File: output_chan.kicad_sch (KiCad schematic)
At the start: 12 parts, among them U4 MAX14917AFM+

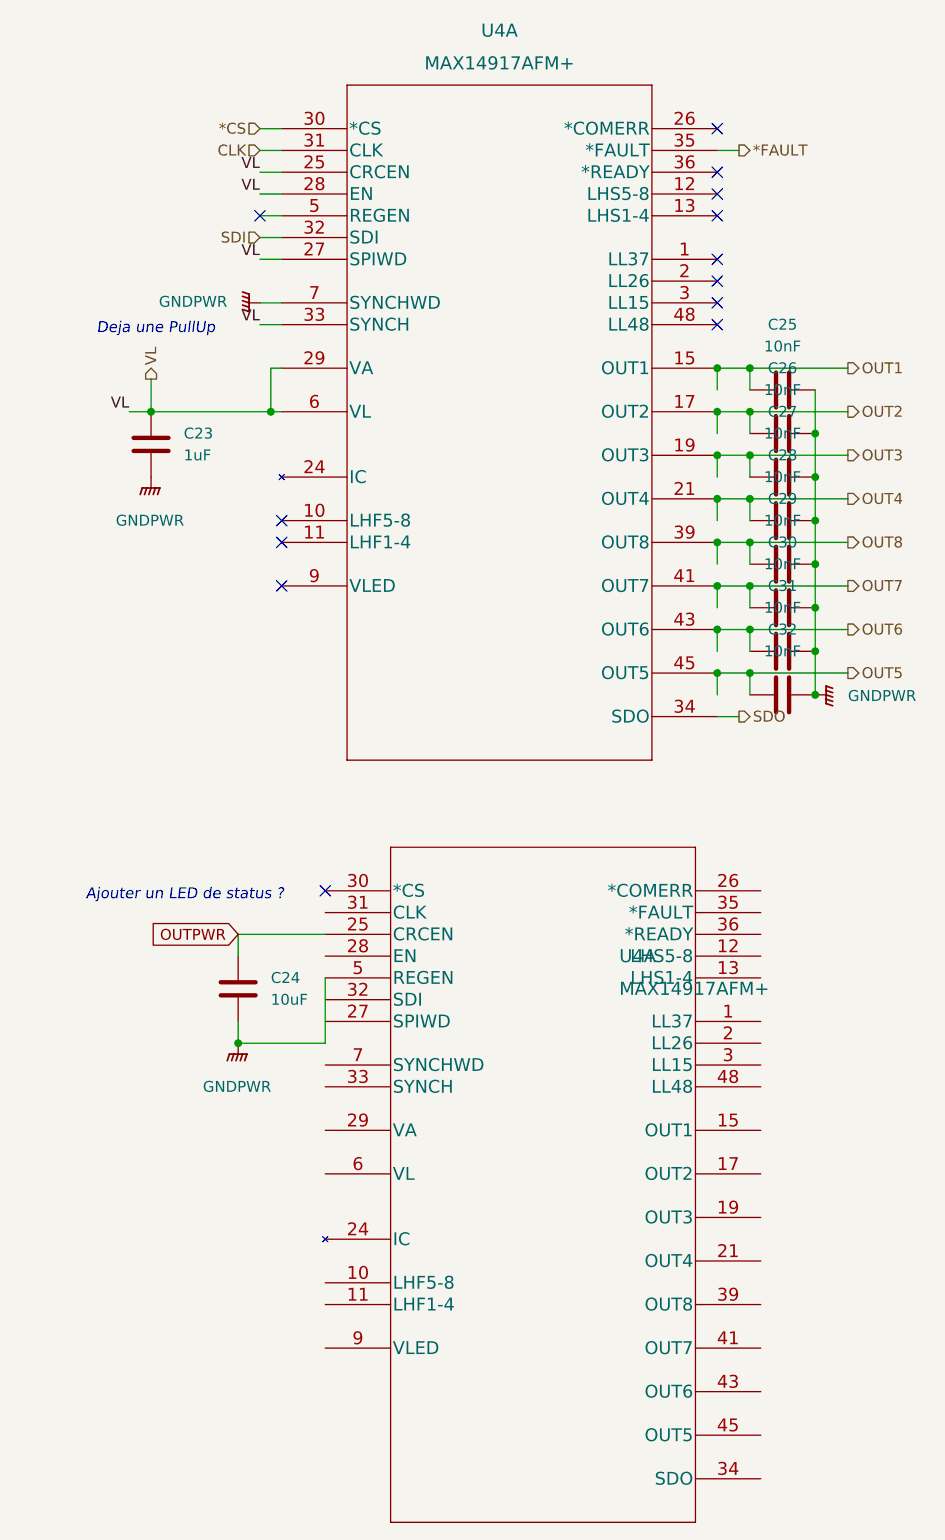
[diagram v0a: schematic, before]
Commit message: add MPGA and MPGB on a DB25 (isolated)
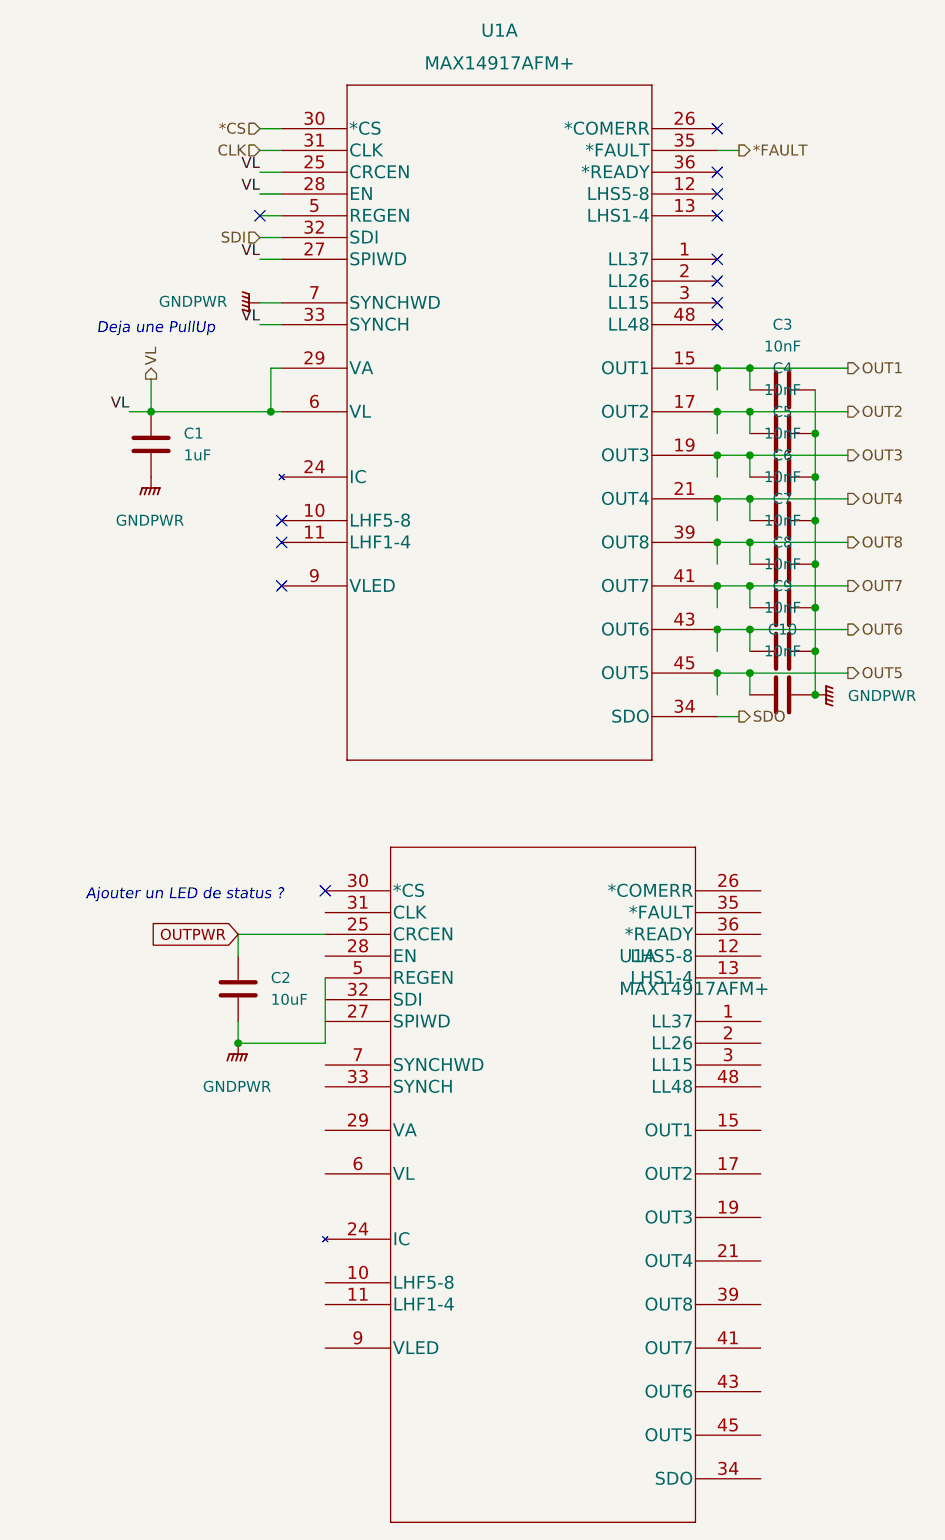
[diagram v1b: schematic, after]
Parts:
- renumbered C23 to C1, C32 to C10, C24 to C2, C25 to C3, C26 to C4, C27 to C5, C28 to C6, C29 to C7, C30 to C8, C31 to C9, U4 to U1
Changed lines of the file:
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@@
   (symbol (lib_id "power:GNDPWR") (at 189.23 109.22 90)
     (in_bom yes) (on_board yes) (fields_autoplaced)
-    (property "Reference" "#PWR023" (id 0) (at 194.31 109.22 0)
+    (property "Reference" "#PWR04" (id 0) (at 194.31 109.22 0)
       (effects (font (size 1.27 1.27)) hide)
     )
@@
   (symbol (lib_id "Device:C") (at 111.76 80.01 0)
     (in_bom yes) (on_board yes) (fields_autoplaced)
-    (property "Reference" "C23" (id 0) (at 115.57 78.7399 0)
+    (property "Reference" "C1" (id 0) (at 115.57 78.7399 0)
       (effects (font (size 1.27 1.27)) (justify left))
     )
@@
   (symbol (lib_id "power:GNDPWR") (at 111.76 83.82 0)
     (in_bom yes) (on_board yes) (fields_autoplaced)
-    (property "Reference" "#PWR020" (id 0) (at 111.76 88.9 0)
+    (property "Reference" "#PWR01" (id 0) (at 111.76 88.9 0)
       (effects (font (size 1.27 1.27)) hide)
     )
@@
   (symbol (lib_id "Maxim industrial IO:MAX14917AFM+") (at 127 43.18 0)
     (in_bom yes) (on_board yes) (fields_autoplaced)
-    (property "Reference" "U4" (id 0) (at 152.4 31.75 0)
+    (property "Reference" "U1" (id 0) (at 152.4 31.75 0)
       (effects (font (size 1.524 1.524)))
     )
@@
   (symbol (lib_id "Device:C") (at 185.42 83.82 90)
     (in_bom yes) (on_board yes) (fields_autoplaced)
-    (property "Reference" "C27" (id 0) (at 185.42 76.2 90))
+    (property "Reference" "C5" (id 0) (at 185.42 76.2 90))
     (property "Value" "10nF" (id 1) (at 185.42 78.74 90))
     (property "Footprint" "Capacitor_SMD:C_0603_1608Metric" (id 2) (at 189.23 82.8548 0)
@@
   (symbol (lib_id "Device:C") (at 185.42 88.9 90)
     (in_bom yes) (on_board yes) (fields_autoplaced)
-    (property "Reference" "C28" (id 0) (at 185.42 81.28 90))
+    (property "Reference" "C6" (id 0) (at 185.42 81.28 90))
     (property "Value" "10nF" (id 1) (at 185.42 83.82 90))
     (property "Footprint" "Capacitor_SMD:C_0603_1608Metric" (id 2) (at 189.23 87.9348 0)
@@
   (symbol (lib_id "Device:C") (at 185.42 78.74 90)
     (in_bom yes) (on_board yes) (fields_autoplaced)
-    (property "Reference" "C26" (id 0) (at 185.42 71.12 90))
+    (property "Reference" "C4" (id 0) (at 185.42 71.12 90))
     (property "Value" "10nF" (id 1) (at 185.42 73.66 90))
     (property "Footprint" "Capacitor_SMD:C_0603_1608Metric" (id 2) (at 189.23 77.7748 0)
@@
   (symbol (lib_id "Device:C") (at 185.42 104.14 90)
     (in_bom yes) (on_board yes) (fields_autoplaced)
-    (property "Reference" "C31" (id 0) (at 185.42 96.52 90))
+    (property "Reference" "C9" (id 0) (at 185.42 96.52 90))
     (property "Value" "10nF" (id 1) (at 185.42 99.06 90))
     (property "Footprint" "Capacitor_SMD:C_0603_1608Metric" (id 2) (at 189.23 103.1748 0)
@@
   (symbol (lib_id "power:GNDPWR") (at 124.46 63.5 270)
     (in_bom yes) (on_board yes) (fields_autoplaced)
-    (property "Reference" "#PWR022" (id 0) (at 119.38 63.5 0)
+    (property "Reference" "#PWR03" (id 0) (at 119.38 63.5 0)
       (effects (font (size 1.27 1.27)) hide)
     )
@@
   (symbol (lib_id "Maxim industrial IO:MAX14917AFM+") (at 132.08 132.08 0)
     (in_bom yes) (on_board yes) (fields_autoplaced)
-    (property "Reference" "U4" (id 0) (at 166.37 139.7 0)
+    (property "Reference" "U1" (id 0) (at 166.37 139.7 0)
       (effects (font (size 1.524 1.524)) (justify left))
     )
@@
   (symbol (lib_id "Device:C") (at 185.42 93.98 90)
     (in_bom yes) (on_board yes) (fields_autoplaced)
-    (property "Reference" "C29" (id 0) (at 185.42 86.36 90))
+    (property "Reference" "C7" (id 0) (at 185.42 86.36 90))
     (property "Value" "10nF" (id 1) (at 185.42 88.9 90))
     (property "Footprint" "Capacitor_SMD:C_0603_1608Metric" (id 2) (at 189.23 93.0148 0)
@@
   (symbol (lib_id "Device:C") (at 185.42 73.66 90)
     (in_bom yes) (on_board yes) (fields_autoplaced)
-    (property "Reference" "C25" (id 0) (at 185.42 66.04 90))
+    (property "Reference" "C3" (id 0) (at 185.42 66.04 90))
     (property "Value" "10nF" (id 1) (at 185.42 68.58 90))
     (property "Footprint" "Capacitor_SMD:C_0603_1608Metric" (id 2) (at 189.23 72.6948 0)
@@
   (symbol (lib_id "Device:C") (at 185.42 99.06 90)
     (in_bom yes) (on_board yes) (fields_autoplaced)
-    (property "Reference" "C30" (id 0) (at 185.42 91.44 90))
+    (property "Reference" "C8" (id 0) (at 185.42 91.44 90))
     (property "Value" "10nF" (id 1) (at 185.42 93.98 90))
     (property "Footprint" "Capacitor_SMD:C_0603_1608Metric" (id 2) (at 189.23 98.0948 0)
@@
   (symbol (lib_id "power:GNDPWR") (at 121.92 149.86 0)
     (in_bom yes) (on_board yes) (fields_autoplaced)
-    (property "Reference" "#PWR021" (id 0) (at 121.92 154.94 0)
+    (property "Reference" "#PWR02" (id 0) (at 121.92 154.94 0)
       (effects (font (size 1.27 1.27)) hide)
     )
@@
   (symbol (lib_id "Device:C") (at 121.92 143.51 0)
     (in_bom yes) (on_board yes) (fields_autoplaced)
-    (property "Reference" "C24" (id 0) (at 125.73 142.2399 0)
+    (property "Reference" "C2" (id 0) (at 125.73 142.2399 0)
       (effects (font (size 1.27 1.27)) (justify left))
     )
@@
   (symbol (lib_id "Device:C") (at 185.42 109.22 90)
     (in_bom yes) (on_board yes) (fields_autoplaced)
-    (property "Reference" "C32" (id 0) (at 185.42 101.6 90))
+    (property "Reference" "C10" (id 0) (at 185.42 101.6 90))
     (property "Value" "10nF" (id 1) (at 185.42 104.14 90))
     (property "Footprint" "Capacitor_SMD:C_0603_1608Metric" (id 2) (at 189.23 108.2548 0)

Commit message: add condo for MPG isolator + small rerouting pair diff
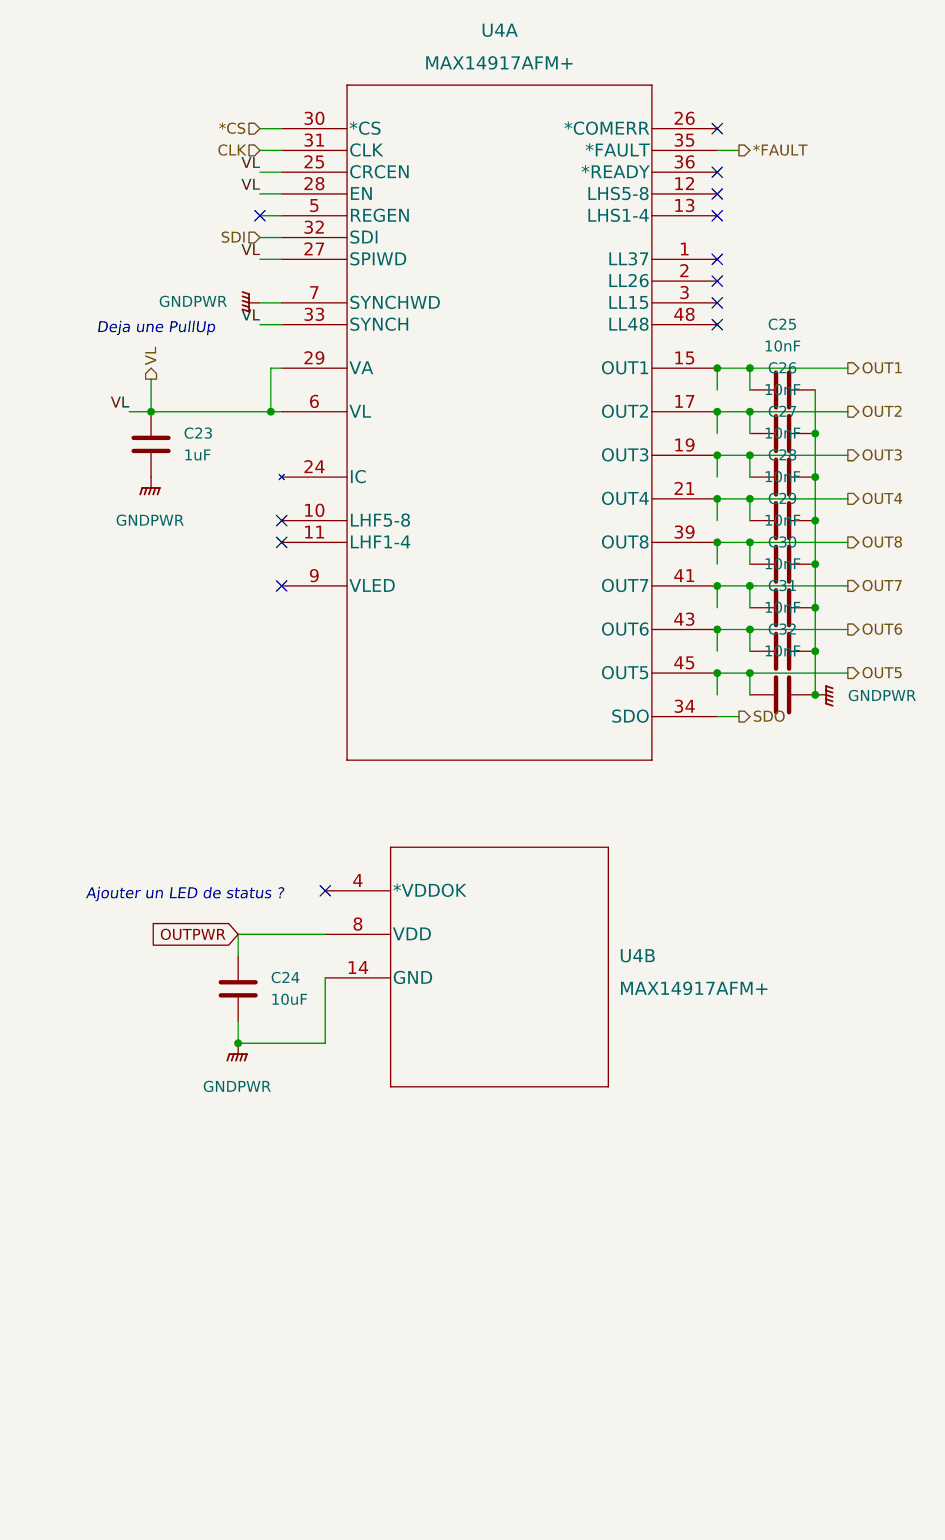
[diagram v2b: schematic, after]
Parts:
- renumbered C1 to C23, C2 to C24, C3 to C25, C4 to C26, C5 to C27, C6 to C28, C7 to C29, C8 to C30, C9 to C31, C10 to C32, U1 to U4
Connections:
- net GNDPWR: now also U4.14 (GND), U4.23 (GND), U4.38 (GND), U4.47 (GND); no longer U4.5 (REGEN)
- net OUTPWR: now also U4.49 (EPAD), U4.8 (VDD); no longer U4.25 (CRCEN)

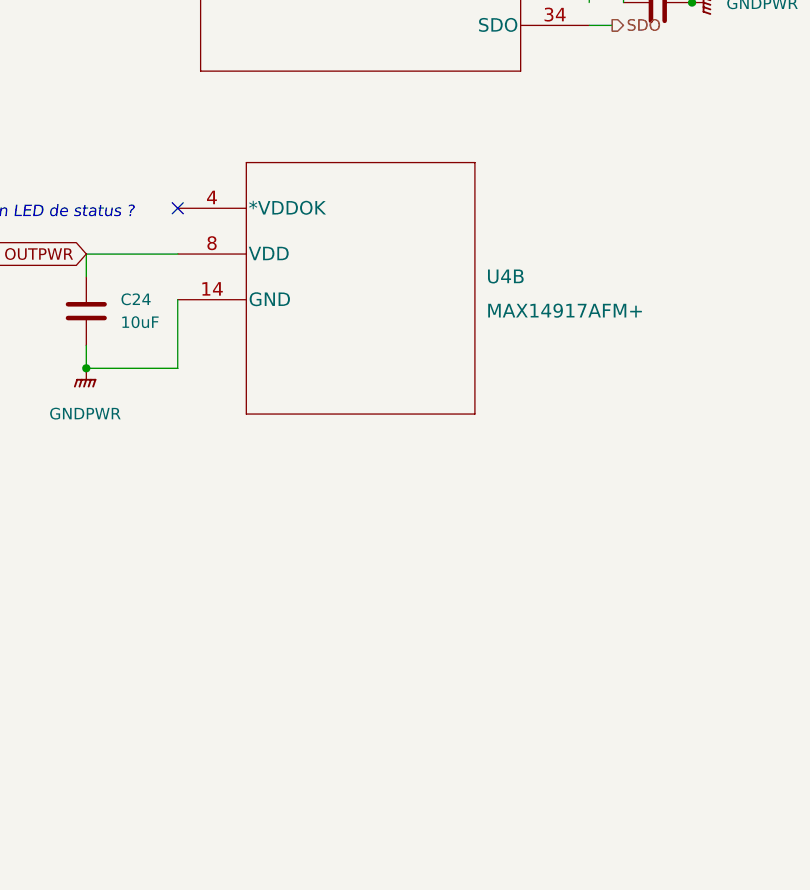
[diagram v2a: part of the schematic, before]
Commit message: add zeners in the meantime, if the SPI isolator is delayed
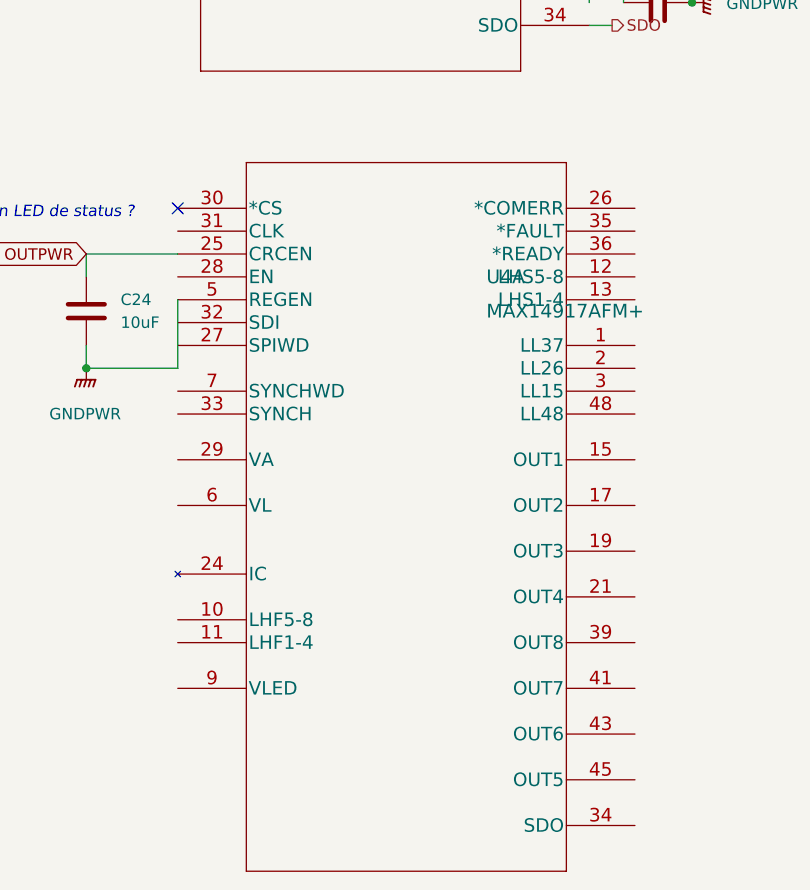
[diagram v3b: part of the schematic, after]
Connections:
- net GNDPWR: now also U4.5 (REGEN); no longer U4.14 (GND), U4.23 (GND), U4.38 (GND), U4.47 (GND)
- net OUTPWR: now also U4.25 (CRCEN); no longer U4.49 (EPAD), U4.8 (VDD)
- new net: U4.15 (OUT1), U4.16 (OUT1)
- new net: U4.17 (OUT2), U4.18 (OUT2)
- new net: U4.19 (OUT3), U4.20 (OUT3)
- new net: U4.21 (OUT4), U4.22 (OUT4)
- new net: U4.37 (VL), U4.6 (VL)
- new net: U4.39 (OUT8), U4.40 (OUT8)
- new net: U4.41 (OUT7), U4.42 (OUT7)
- new net: U4.43 (OUT6), U4.44 (OUT6)
- new net: U4.45 (OUT5), U4.46 (OUT5)
